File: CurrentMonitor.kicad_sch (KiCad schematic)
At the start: 9 parts

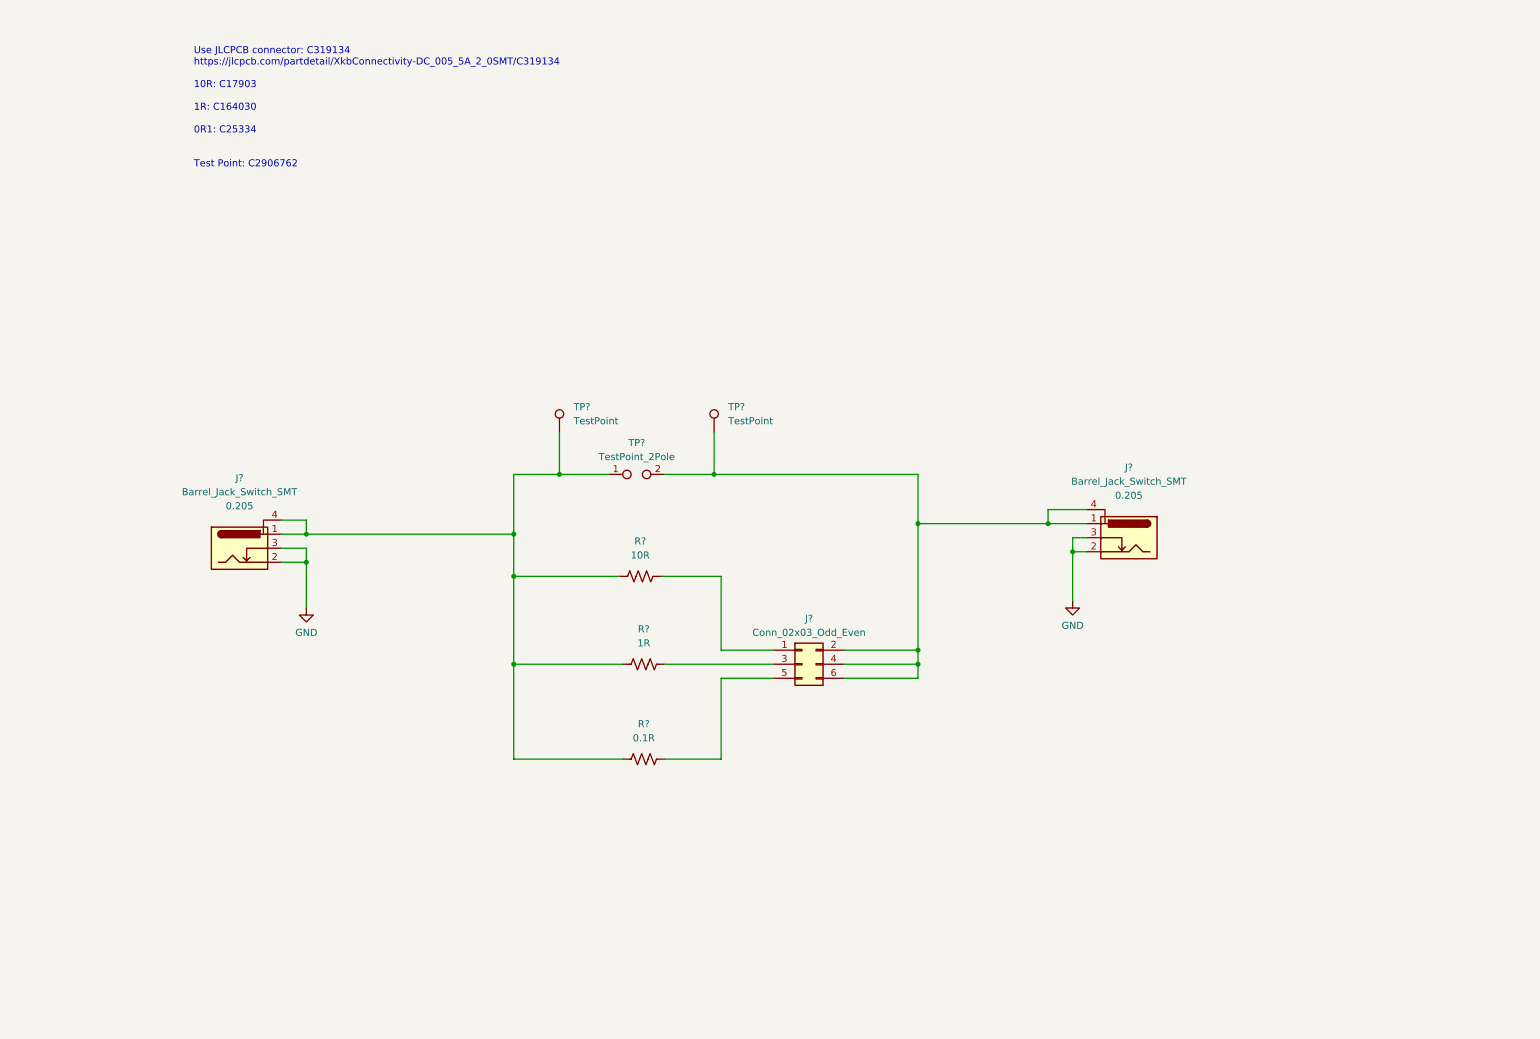
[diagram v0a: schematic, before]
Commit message: Add design rule check custom check.
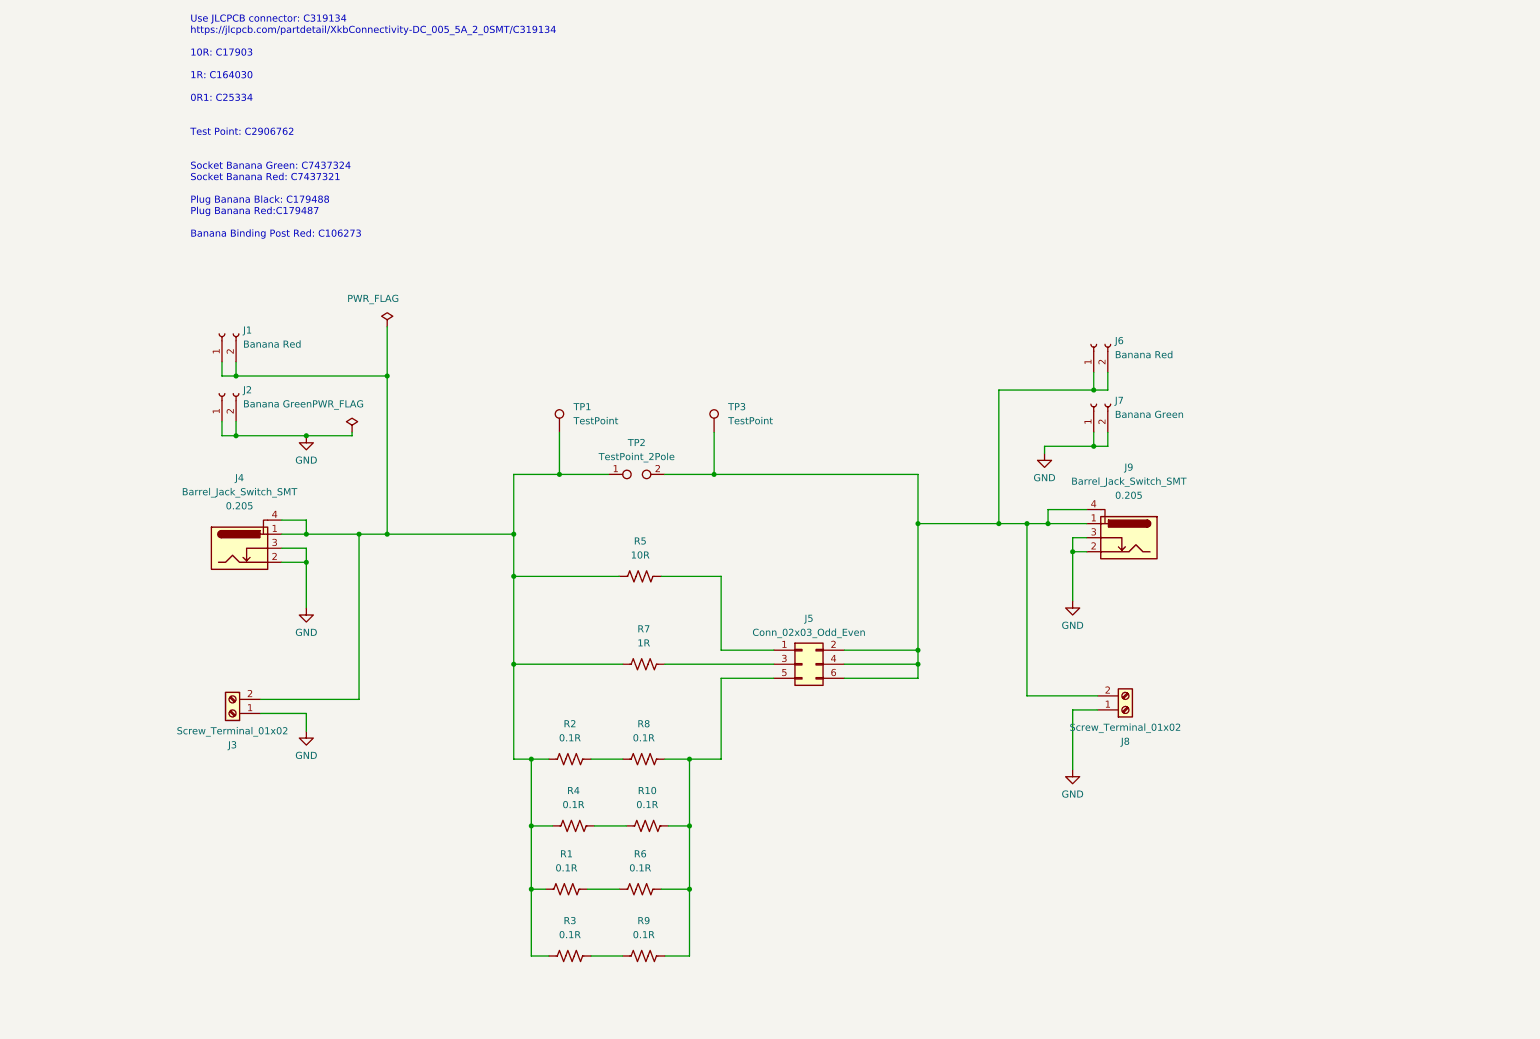
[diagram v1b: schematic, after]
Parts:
- added J1, J6: Banana Red, symbol Connector:Conn_01x02_Socket
- added J2, J7: Banana Green, symbol Connector:Conn_01x02_Socket
- added J3, J8: Screw_Terminal_01x02, symbol Connector:Screw_Terminal_01x02
- added R1, R10, R2, R3, R4, R6, R9: 0.1R, symbol Device:R_US
- J5: renamed from J?; Distributor 1 (none) -> JLCPCB; Distributor 1 PN (none) -> C5116479
- R5: renamed from R?; Distributor 1 (none) -> JLCPCB; Distributor 1 PN (none) -> C17903
- R7: renamed from R?; Distributor 1 (none) -> JLCPCB; Distributor 1 PN (none) -> C164030
- R8: renamed from R?; Distributor 1 (none) -> JLCPCB; Distributor 1 PN (none) -> C25334
- TP1, TP3: renamed from TP?; Distributor 1 (none) -> JLCPCB; Distributor 1 PN (none) -> C2906762
- TP2: renamed from TP?; Distributor 1 (none) -> JLCPCB
- gave numbers to parts that had none: 2
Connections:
- net GND: now also J2.1 (Pin_1), J2.2 (Pin_2), J3.1 (Pin_1), J7.1 (Pin_1), J7.2 (Pin_2), J8.1 (Pin_1)
- net at J4.1, J4.4, R5.1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: now also J1.1 (Pin_1), J1.2 (Pin_2), J3.2 (Pin_2), R1.1, R2.1, R3.1, R4.1; no longer R8.1
- net at J5.2 (Pin_2), J5.4 (Pin_4), J5.6 (Pin_6)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: now also J6.1 (Pin_1), J6.2 (Pin_2), J8.2 (Pin_2)
- net at J5.5 (Pin_5), R8.2: now also R10.2, R6.2, R9.2
- new net: R1.2, R6.1
- new net: R3.2, R9.1
- new net: R10.1, R4.2
- new net: R2.2, R8.1
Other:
- note added: "Use JLCPCB connector: C319134 https://jlcpcb.com/partdetail/XkbConnectivity-DC_005_5A_2_0SMT/C319134 10R: C17903 1R: C164030 0R1: C25334 Test Point: C2906762 Socket Banana Green: C7437324 Socket Banana Red: C7437321 Plug Banana Black: C179488 Plug Banana Red:C179487 Banana Binding Post Red: C106273"
- note removed: "Use JLCPCB connector: C319134 https://jlcpcb.com/partdetail/XkbConnectivity-DC_005_5A_2_0SMT/C319134 10R: C17903 1R: C164030 0R1: C25334 Test Point: C2906762"

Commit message: Add more JLCPCB parts, banana jacks and more.
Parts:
- added J5: Screw_Terminal_01x02, symbol Connector:Screw_Terminal_01x02
- renumbered J9 to J10, J5 to J6, J6 to J7, J7 to J8, J8 to J9
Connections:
- net at J1.1 (Pin_1), J1.2 (Pin_2), J3.2 (Pin_2)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: now also J5.2 (Pin_2)
- net at J10.1, J10.4, J6.2 (Pin_2)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: now also J5.1 (Pin_1)
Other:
- note added: "Use JLCPCB Parts Where Possible Panel Mounting DC Power Receptacle: C319134 10R: C17903 1R: C164030 0R1: C25334 Test Point: C2906762 Socket Banana Green: C7437324 Socket Banana Red: C7437321 Plug Banana Black: C179488 Plug Banana Red:C179487 Banana Binding Post Red: C106273 Banana Binding Post Green: ???? Banana Binding Post Yellow: C309375 Banana Binding Post Black: C106272"
- note removed: "Use JLCPCB connector: C319134 https://jlcpcb.com/partdetail/XkbConnectivity-DC_005_5A_2_0SMT/C319134 10R: C17903 1R: C164030 0R1: C25334 Test Point: C2906762 Socket Banana Green: C7437324 Socket Banana Red: C7437321 Plug Banana Black: C179488 Plug Banana Red:C179487 Banana Binding Post Red: C106273"
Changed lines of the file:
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@@
   (junction (at 58.42 88.9) (diameter 0) (color 0 0 0 0)
   )
+  (junction (at 108.585 95.885) (diameter 0) (color 0 0 0 0)
+  )
   (junction (at 201.295 104.775) (diameter 0) (color 0 0 0 0)
   )
@@
   (junction (at 181.61 130.175) (diameter 0) (color 0 0 0 0)
   )
+  (junction (at 181.61 95.885) (diameter 0) (color 0 0 0 0)
+  )
   (junction (at 111.76 147.32) (diameter 0) (color 0 0 0 0)
   )
@@
     (stroke (width 0) (type default))
   )
+  (wire (pts (xy 108.585 69.215) (xy 108.585 95.885))
+    (stroke (width 0) (type default))
+  )
   (wire (pts (xy 146.05 147.32) (xy 140.335 147.32))
     (stroke (width 0) (type default))
@@
     (stroke (width 0) (type default))
   )
+  (wire (pts (xy 181.61 69.215) (xy 181.61 95.885))
+    (stroke (width 0) (type default))
+  )
   (wire (pts (xy 55.88 86.36) (xy 55.88 88.9))
     (stroke (width 0) (type default))
@@
     (stroke (width 0) (type default))
   )
+  (wire (pts (xy 128.905 69.215) (xy 108.585 69.215))
+    (stroke (width 0) (type default))
+  )
   (wire (pts (xy 58.42 88.9) (xy 71.12 88.9))
     (stroke (width 0) (type default))
@@
     (stroke (width 0) (type default))
   )
+  (wire (pts (xy 131.445 69.215) (xy 181.61 69.215))
+    (stroke (width 0) (type default))
+  )
   (wire (pts (xy 140.335 147.32) (xy 140.335 159.385))
     (stroke (width 0) (type default))
@@
     (stroke (width 0) (type default))
   )
-  (text "Use JLCPCB connector: C319134\nhttps://jlcpcb.com/partdetail/XkbConnectivity-DC_005_5A_2_0SMT/C319134\n\n10R: C17903\n\n1R: C164030\n\n0R1: C25334\n\n\nTest Point: C2906762\n\n\nSocket Banana Green: C7437324\nSocket Banana Red: C7437321\n\nPlug Banana Black: C179488\nPlug Banana Red:C179487\n\nBanana Binding Post Red: C106273"
+  (text "Use JLCPCB Parts Where Possible\n\nPanel Mounting DC Power Receptacle: C319134\n\n10R: C17903\n1R: C164030\n0R1: C25334\n\nTest Point: C2906762\n\nSocket Banana Green: C7437324\nSocket Banana Red: C7437321\n\nPlug Banana Black: C179488\nPlug Banana Red:C179487\n\nBanana Binding Post Red: C106273\nBanana Binding Post Green: ????\nBanana Binding Post Yellow: C309375\nBanana Binding Post Black: C106272"
     (at 50.165 53.34 0)
     (effects (font (size 1.27 1.27)) (justify left bottom))
@@
   (symbol (lib_id "Connector:Conn_01x02_Socket") (at 213.36 72.39 90) (unit 1)
     (in_bom yes) (on_board yes) (dnp no) (fields_autoplaced)
-    (property "Reference" "J6" (at 217.17 71.755 90)
+    (property "Reference" "J7" (at 217.17 71.755 90)
       (effects (font (size 1.27 1.27)) (justify right))
     )
@@
       (project "CurrentMonitor"
         (path "/c2625580-5dc2-4487-938a-c703153fa89f"
-          (reference "J6") (unit 1)
+          (reference "J7") (unit 1)
         )
       )
@@
   (symbol (lib_id "power:GND") (at 71.12 120.015 0) (unit 1)
     (in_bom yes) (on_board yes) (dnp no) (fields_autoplaced)
-    (property "Reference" "#PWR01" (at 71.12 126.365 0)
+    (property "Reference" "#PWR02" (at 71.12 126.365 0)
       (effects (font (size 1.27 1.27)) hide)
     )
@@
       (project "CurrentMonitor"
         (path "/c2625580-5dc2-4487-938a-c703153fa89f"
-          (reference "#PWR01") (unit 1)
+          (reference "#PWR02") (unit 1)
         )
       )
@@
       (project "CurrentMonitor"
         (path "/c2625580-5dc2-4487-938a-c703153fa89f"
-          (reference "#FLG01") (unit 1)
+          (reference "#FLG02") (unit 1)
         )
       )
@@
   (symbol (lib_id "Connector_Generic:Conn_02x03_Odd_Even") (at 160.655 130.175 0) (unit 1)
     (in_bom yes) (on_board yes) (dnp no) (fields_autoplaced)
-    (property "Reference" "J5" (at 161.925 121.92 0)
+    (property "Reference" "J6" (at 161.925 121.92 0)
       (effects (font (size 1.27 1.27)))
     )
@@
       (project "CurrentMonitor"
         (path "/c2625580-5dc2-4487-938a-c703153fa89f"
-          (reference "J5") (unit 1)
+          (reference "J6") (unit 1)
         )
       )
@@
   (symbol (lib_id "Connector:Screw_Terminal_01x02") (at 219.075 138.43 0) (mirror x) (unit 1)
     (in_bom yes) (on_board yes) (dnp no)
-    (property "Reference" "J8" (at 219.075 144.145 0)
+    (property "Reference" "J9" (at 219.075 144.145 0)
       (effects (font (size 1.27 1.27)))
     )
@@
       (project "CurrentMonitor"
         (path "/c2625580-5dc2-4487-938a-c703153fa89f"
-          (reference "J8") (unit 1)
+          (reference "J9") (unit 1)
         )
       )
@@
   (symbol (lib_id "PubInv_KiCad_SCH_LIB:Barrel_Jack_Switch_SMT") (at 219.71 107.315 0) (mirror y) (unit 1)
     (in_bom yes) (on_board yes) (dnp no)
-    (property "Reference" "J9" (at 219.71 94.615 0)
+    (property "Reference" "J10" (at 219.71 94.615 0)
       (effects (font (size 1.27 1.27)))
     )
@@
       (project "CurrentMonitor"
         (path "/c2625580-5dc2-4487-938a-c703153fa89f"
-          (reference "J9") (unit 1)
+          (reference "J10") (unit 1)
         )
       )
@@
   (symbol (lib_id "power:GND") (at 204.47 92.075 0) (unit 1)
     (in_bom yes) (on_board yes) (dnp no) (fields_autoplaced)
-    (property "Reference" "#PWR06" (at 204.47 98.425 0)
+    (property "Reference" "#PWR04" (at 204.47 98.425 0)
       (effects (font (size 1.27 1.27)) hide)
     )
@@
       (project "CurrentMonitor"
         (path "/c2625580-5dc2-4487-938a-c703153fa89f"
-          (reference "#PWR06") (unit 1)
+          (reference "#PWR04") (unit 1)
         )
       )
@@
   (symbol (lib_id "power:GND") (at 209.55 118.745 0) (unit 1)
     (in_bom yes) (on_board yes) (dnp no) (fields_autoplaced)
-    (property "Reference" "#PWR02" (at 209.55 125.095 0)
+    (property "Reference" "#PWR05" (at 209.55 125.095 0)
       (effects (font (size 1.27 1.27)) hide)
     )
@@
       (project "CurrentMonitor"
         (path "/c2625580-5dc2-4487-938a-c703153fa89f"
-          (reference "#PWR02") (unit 1)
+          (reference "#PWR05") (unit 1)
+        )
+      )
+    )
+  )
+  (symbol (lib_id "Connector:Screw_Terminal_01x02") (at 131.445 64.135 270) (mirror x) (unit 1)
+    (in_bom yes) (on_board yes) (dnp no)
+    (property "Reference" "J5" (at 137.16 64.135 0)
+      (effects (font (size 1.27 1.27)))
+    )
+    (property "Value" "Screw_Terminal_01x02" (at 134.62 64.135 0)
+      (effects (font (size 1.27 1.27)))
+    )
+    (property "Footprint" "" (at 131.445 64.135 0)
+      (effects (font (size 1.27 1.27)) hide)
+    )
+    (property "Datasheet" "~" (at 131.445 64.135 0)
+      (effects (font (size 1.27 1.27)) hide)
+    )
+    (property "Distributor 1" "JLCPCB" (at 131.445 64.135 0)
+      (effects (font (size 1.27 1.27)) hide)
+    )
+    (property "Distributor 1 PN" "C8385" (at 131.445 64.135 0)
+      (effects (font (size 1.27 1.27)) hide)
+    )
+    (pin "1")
+    (pin "2")
+    (instances
+      (project "CurrentMonitor"
+        (path "/c2625580-5dc2-4487-938a-c703153fa89f"
+          (reference "J5") (unit 1)
         )
       )
@@
       (project "CurrentMonitor"
         (path "/c2625580-5dc2-4487-938a-c703153fa89f"
-          (reference "#FLG02") (unit 1)
+          (reference "#FLG01") (unit 1)
         )
       )
@@
   (symbol (lib_id "power:GND") (at 71.12 88.9 0) (unit 1)
     (in_bom yes) (on_board yes) (dnp no) (fields_autoplaced)
-    (property "Reference" "#PWR05" (at 71.12 95.25 0)
+    (property "Reference" "#PWR01" (at 71.12 95.25 0)
       (effects (font (size 1.27 1.27)) hide)
     )
@@
       (project "CurrentMonitor"
         (path "/c2625580-5dc2-4487-938a-c703153fa89f"
-          (reference "#PWR05") (unit 1)
+          (reference "#PWR01") (unit 1)
         )
       )
@@
   (symbol (lib_id "Connector:Conn_01x02_Socket") (at 213.36 83.185 90) (unit 1)
     (in_bom yes) (on_board yes) (dnp no) (fields_autoplaced)
-    (property "Reference" "J7" (at 217.17 82.55 90)
+    (property "Reference" "J8" (at 217.17 82.55 90)
       (effects (font (size 1.27 1.27)) (justify right))
     )
@@
       (project "CurrentMonitor"
         (path "/c2625580-5dc2-4487-938a-c703153fa89f"
-          (reference "J7") (unit 1)
+          (reference "J8") (unit 1)
         )
       )
@@
   (symbol (lib_id "power:GND") (at 209.55 149.225 0) (unit 1)
     (in_bom yes) (on_board yes) (dnp no) (fields_autoplaced)
-    (property "Reference" "#PWR04" (at 209.55 155.575 0)
+    (property "Reference" "#PWR06" (at 209.55 155.575 0)
       (effects (font (size 1.27 1.27)) hide)
     )
@@
       (project "CurrentMonitor"
         (path "/c2625580-5dc2-4487-938a-c703153fa89f"
-          (reference "#PWR04") (unit 1)
-        )
-      )
+          (reference "#PWR06") (unit 1)
+        )
+      )

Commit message: Add USB connectors, BNC for oscilliscope monitor.
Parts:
- added J1: USB_B_Micro, symbol Connector:USB_B_Micro
- added J12: USB_A, symbol Connector:USB_A
- added J13: Conn_Coaxial, symbol Connector:Conn_Coaxial
- added TP1: TestPoint, symbol Connector:TestPoint
- renumbered J9 to J10, J10 to J11, J1 to J2, J2 to J3, J3 to J5, J5 to J6, J6 to J7, J7 to J8, J8 to J9, TP1 to TP2, TP2 to TP3, TP3 to TP4
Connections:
- net GND: now also J1.5 (GND), J1.6 (Shield), J12.4 (GND), J12.5 (Shield), J13.2 (Ext)
- net at J2.1 (Pin_1), J2.2 (Pin_2), J4.1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: now also J1.1 (VBUS)
- net at J10.2 (Pin_2), J11.1, J11.4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: now also J12.1 (VBUS), J13.1 (In)
- new net: J1.2 (D-), J12.2 (D-)
- new net: J1.3 (D+), J12.3 (D+)
- new net: J1.4 (ID), TP1.1
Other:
- note added: "Move jumpter to select burden resistor."
- note added: "To multimeter to monitor current."
- note added: "To oscilliscope to monitor ripple."
- moved on the sheet: J5
